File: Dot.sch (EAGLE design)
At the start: 37 parts, among them IC1 CAT24M010TS, IC2 SI1145, U1 ATMEGA328P-MU-QFN32, U2 TMP102, U3 ISL29125, U4 9DoF IMU, U5 BMP18

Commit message: Added voltage divider for input voltage measuring.
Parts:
- added R1, R9: (no value), resistor:R-EU_R0603
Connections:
- new net VIN_PIN: JP1.6, R9.2
- net GND: now also R1.1
- net VIN: now also R1.2, R9.1; no longer JP1.6
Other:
- note added: "Added 100uF Cap."
- note added: "Voltage Divider Lower R"
- note removed: "Added 100uF Cap. Should soften discharge of batetry to peaks up to 30mA for 1ms. Reacharges in 175ms."
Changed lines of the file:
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@@
 <setting verticaltext="up"/>
 </settings>
-<grid distance="0.05" unitdist="inch" unit="inch" style="lines" multiple="1" display="no" altdistance="0.01" altunitdist="inch" altunit="inch"/>
+<grid distance="0.1" unitdist="inch" unit="inch" style="lines" multiple="1" display="no" altdistance="0.01" altunitdist="inch" altunit="inch"/>
 <layers>
 <layer number="1" name="Top" color="4" fill="1" visible="no" active="no"/>
@@
 <part name="SJ2" library="SparkFun" deviceset="SOLDERJUMPER" device="TRACE"/>
 <part name="C5" library="Seeed-OPL-Capacitor" deviceset="TANTALUM-SMD-100UF-6.3V(AVX-A)" device="" value="100uf"/>
+<part name="R1" library="resistor" deviceset="R-EU_" device="R0603"/>
+<part name="SUPPLY16" library="supply2" deviceset="GND" device=""/>
+<part name="R9" library="resistor" deviceset="R-EU_" device="R0603"/>
 </parts>
 <sheets>
@@
 <text x="-7.62" y="50.8" size="1.27" layer="91" rot="R90">Green</text>
 <text x="1.778" y="50.8" size="1.27" layer="91">Red</text>
+<text x="-60.96" y="134.62" size="1.778" layer="91">Voltage Divider Lower R</text>
 </plain>
 <instances>
@@
 <instance part="SJ2" gate="1" x="284.48" y="68.58"/>
 <instance part="C5" gate="G$1" x="2.54" y="162.56" rot="R270"/>
+<instance part="R1" gate="G$1" x="-33.02" y="134.62" rot="R90"/>
+<instance part="SUPPLY16" gate="GND" x="-33.02" y="127"/>
+<instance part="R9" gate="G$1" x="-33.02" y="147.32" rot="R90"/>
 </instances>
 <busses>
@@
 <wire x1="2.54" y1="158.75" x2="10.16" y2="158.75" width="0.1524" layer="91"/>
 <junction x="10.16" y="158.75"/>
+</segment>
+<segment>
+<pinref part="R1" gate="G$1" pin="1"/>
+<pinref part="SUPPLY16" gate="GND" pin="GND"/>
 </segment>
 </net>
@@
 </segment>
 <segment>
-<pinref part="JP1" gate="A" pin="6"/>
-<wire x1="73.66" y1="132.08" x2="86.36" y2="132.08" width="0.1524" layer="91"/>
-<label x="86.36" y="132.08" size="1.27" layer="95" xref="yes"/>
+<pinref part="R9" gate="G$1" pin="1"/>
+<pinref part="R1" gate="G$1" pin="2"/>
+<wire x1="-33.02" y1="142.24" x2="-33.02" y2="139.7" width="0.1524" layer="91"/>
+<wire x1="-33.02" y1="142.24" x2="-27.94" y2="142.24" width="0.1524" layer="91"/>
+<junction x="-33.02" y="142.24"/>
+<label x="-27.94" y="142.24" size="1.27" layer="95" xref="yes"/>
 </segment>
 </net>
@@
 <pinref part="X1" gate="G$1" pin="SIGNAL"/>
 <wire x1="289.56" y1="68.58" x2="292.1" y2="68.58" width="0.1524" layer="91"/>
+</segment>
+</net>
+<net name="VIN_PIN" class="0">
+<segment>
+<pinref part="R9" gate="G$1" pin="2"/>
+<wire x1="-33.02" y1="152.4" x2="-33.02" y2="154.94" width="0.1524" layer="91"/>
+<label x="-33.02" y="154.94" size="1.27" layer="95" xref="yes"/>
+</segment>
+<segment>
+<pinref part="JP1" gate="A" pin="6"/>
+<wire x1="73.66" y1="132.08" x2="86.36" y2="132.08" width="0.1524" layer="91"/>
 </segment>
 </net>
@@
 <text x="-13.97" y="88.9" size="2.54" layer="91">Diff to v1.3</text>
 <text x="-13.462" y="80.01" size="2.1844" layer="91">Corrected RGB Led layout.</text>
-<text x="-12.7" y="73.66" size="2.1844" layer="91">Added 100uF Cap. Should soften discharge of batetry to peaks up to 30mA for 1ms. Reacharges in 175ms.</text>
+<text x="-12.7" y="73.66" size="2.1844" layer="91">Added 100uF Cap.</text>
 </plain>
 <instances>

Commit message: Adding solderjumper for bypassing Voltage Regulator
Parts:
- added SJ3: SOLDERJUMPERNC2, SparkFun:SOLDERJUMPERNC2
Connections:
- net +3V3: now also SJ3.2
- net VIN: now also SJ3.1
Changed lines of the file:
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@@
 <part name="SUPPLY16" library="supply2" deviceset="GND" device=""/>
 <part name="R9" library="resistor" deviceset="R-EU_" device="R0603"/>
+<part name="SJ3" library="SparkFun" deviceset="SOLDERJUMPER" device="NC2"/>
 </parts>
 <sheets>
@@
 RGB Led, Buzzer</text>
 <text x="340.36" y="10.16" size="3.81" layer="95">Antenna Tuning</text>
-<text x="33.02" y="106.68" size="3.81" layer="95">Power and Headers</text>
+<text x="43.18" y="106.68" size="3.81" layer="95">Power and Headers</text>
 <text x="238.76" y="106.68" size="3.81" layer="95">I2C, Reset and Pullups &amp; Push Button(s)</text>
 <text x="-17.78" y="35.56" size="1.778" layer="91">Values @ 20mA.</text>
@@
 <instance part="SUPPLY16" gate="GND" x="-33.02" y="127"/>
 <instance part="R9" gate="G$1" x="-33.02" y="147.32" rot="R90"/>
+<instance part="SJ3" gate="1" x="17.78" y="114.3"/>
 </instances>
 <busses>
@@
 <pinref part="+3V19" gate="G$1" pin="+3V3"/>
 <wire x1="30.48" y1="142.24" x2="30.48" y2="134.62" width="0.1524" layer="91"/>
+<pinref part="SJ3" gate="1" pin="2"/>
+<wire x1="22.86" y1="114.3" x2="30.48" y2="114.3" width="0.1524" layer="91"/>
+<wire x1="30.48" y1="114.3" x2="30.48" y2="134.62" width="0.1524" layer="91"/>
+<junction x="30.48" y="134.62"/>
 </segment>
 <segment>
@@
 <junction x="7.62" y="134.62"/>
 <label x="5.08" y="134.62" size="1.27" layer="95" rot="R180" xref="yes"/>
-</segment>
-<segment>
+<pinref part="SJ3" gate="1" pin="1"/>
+<wire x1="7.62" y1="132.08" x2="7.62" y2="114.3" width="0.1524" layer="91"/>
+<wire x1="7.62" y1="114.3" x2="12.7" y2="114.3" width="0.1524" layer="91"/>
+<junction x="7.62" y="132.08"/>
+</segment>
+<segment>

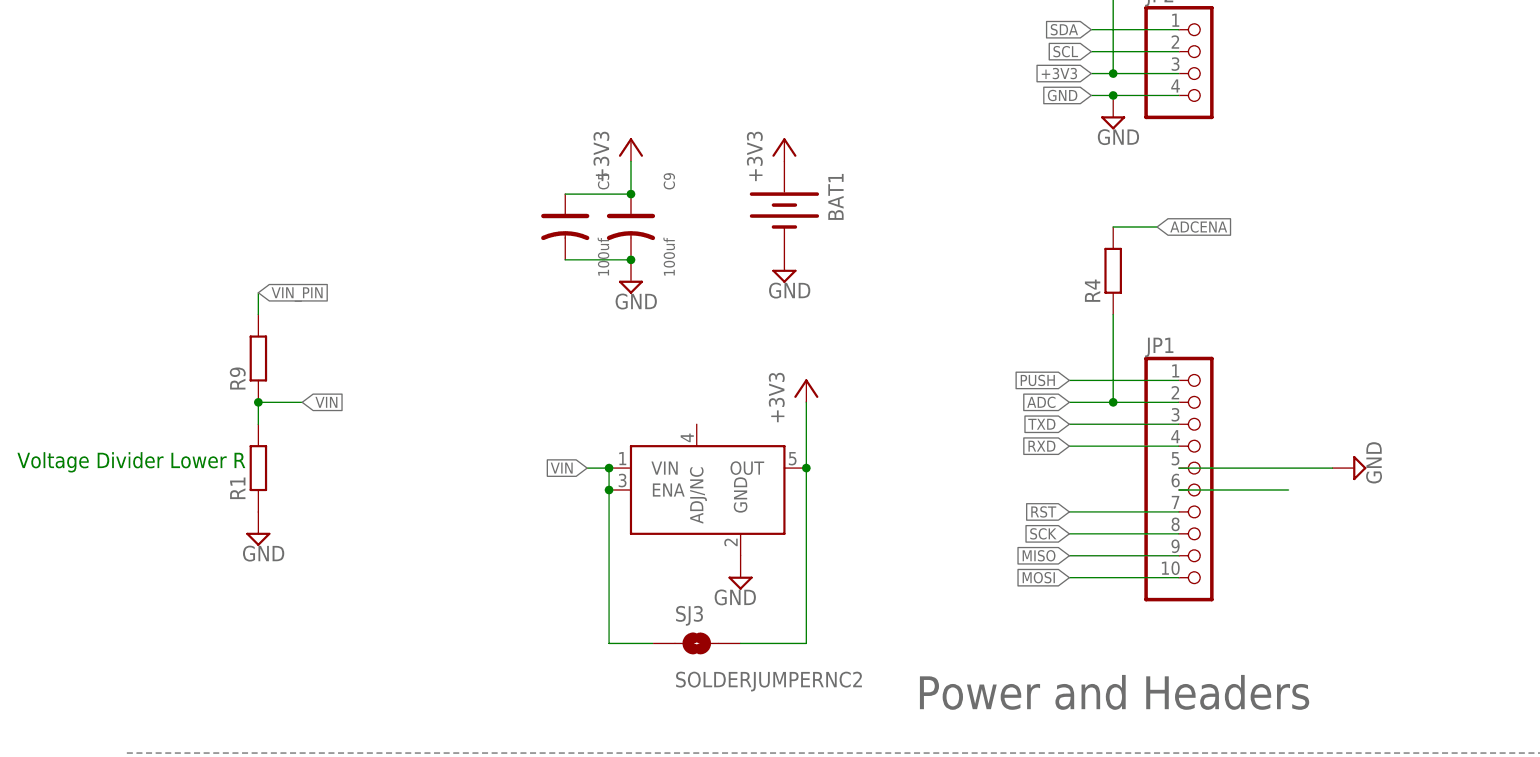
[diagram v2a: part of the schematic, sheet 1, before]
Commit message: Added cap for Reset via DTR pin / Easy Arduino upload
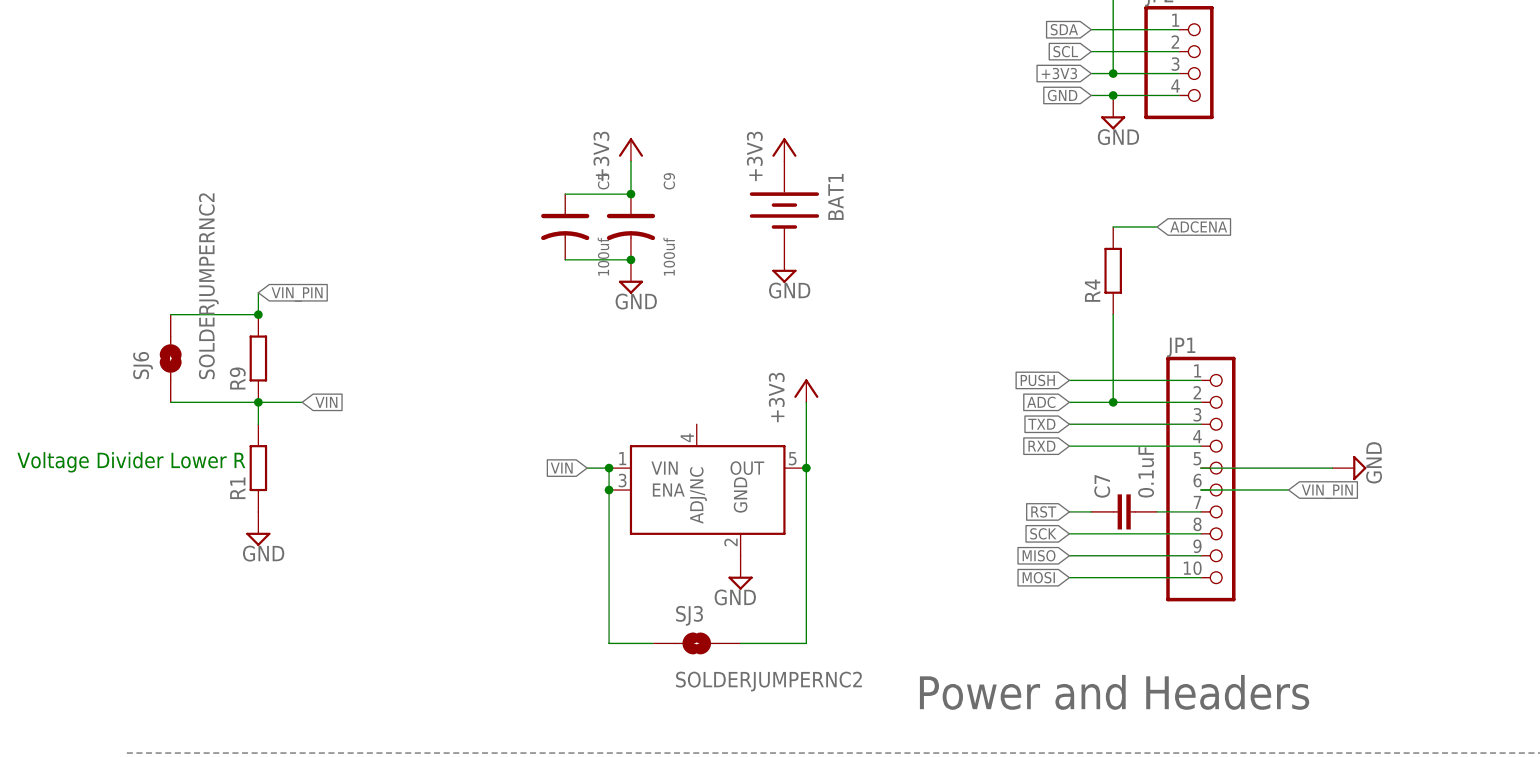
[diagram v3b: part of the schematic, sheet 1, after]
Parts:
- added C7: 0.1uF, resistor:C-EUC0603
- added SJ6: SOLDERJUMPERNC2, SparkFun:SOLDERJUMPERNC2
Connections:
- new net N$5: C7.2, JP1.7
- net RST: now also C7.1; no longer JP1.7
- net VIN: now also SJ6.1
- net VIN_PIN: now also SJ6.2
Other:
- moved on the sheet: JP1
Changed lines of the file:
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@@
 <part name="R9" library="resistor" deviceset="R-EU_" device="R0603"/>
 <part name="SJ3" library="SparkFun" deviceset="SOLDERJUMPER" device="NC2"/>
+<part name="C7" library="resistor" deviceset="C-EU" device="C0603" value="0.1uF"/>
+<part name="SJ6" library="SparkFun" deviceset="SOLDERJUMPER" device="NC2"/>
 </parts>
 <sheets>
@@
 <instance part="SUPPLY13" gate="GND" x="33.02" y="-30.48"/>
 <instance part="SUPPLY19" gate="GND" x="297.18" y="124.46"/>
-<instance part="JP1" gate="A" x="76.2" y="134.62"/>
+<instance part="JP1" gate="A" x="78.74" y="134.62"/>
 <instance part="R5" gate="G$1" x="0" y="60.96" rot="R270"/>
 <instance part="R6" gate="G$1" x="-20.32" y="60.96" rot="R270"/>
@@
 <instance part="R9" gate="G$1" x="-33.02" y="147.32" rot="R90"/>
 <instance part="SJ3" gate="1" x="17.78" y="114.3"/>
+<instance part="C7" gate="G$1" x="66.04" y="129.54" rot="R90"/>
+<instance part="SJ6" gate="1" x="-43.18" y="147.32" rot="R90"/>
 </instances>
 <busses>
@@
 <segment>
 <pinref part="SUPPLY1" gate="GND" pin="GND"/>
-<wire x1="73.66" y1="134.62" x2="91.44" y2="134.62" width="0.1524" layer="91"/>
+<wire x1="76.2" y1="134.62" x2="91.44" y2="134.62" width="0.1524" layer="91"/>
 <pinref part="JP1" gate="A" pin="5"/>
 </segment>
@@
 <net name="RST" class="0">
 <segment>
-<label x="60.96" y="129.54" size="1.27" layer="95" rot="R180" xref="yes"/>
-<wire x1="60.96" y1="129.54" x2="73.66" y2="129.54" width="0.1524" layer="91"/>
-<pinref part="JP1" gate="A" pin="7"/>
-</segment>
-<segment>
 <pinref part="U1" gate="G$1" pin="PC6(PCINT14/!RESET)"/>
 <wire x1="195.58" y1="43.18" x2="198.12" y2="43.18" width="0.1524" layer="91"/>
@@
 <wire x1="269.24" y1="154.94" x2="251.46" y2="154.94" width="0.1524" layer="91"/>
 <label x="251.46" y="154.94" size="1.27" layer="95" rot="R180" xref="yes"/>
+</segment>
+<segment>
+<pinref part="C7" gate="G$1" pin="1"/>
+<wire x1="63.5" y1="129.54" x2="60.96" y2="129.54" width="0.1524" layer="91"/>
+<label x="60.96" y="129.54" size="1.27" layer="95" rot="R180" xref="yes"/>
 </segment>
 </net>
@@
 <segment>
 <label x="60.96" y="121.92" size="1.27" layer="95" rot="R180" xref="yes"/>
-<wire x1="60.96" y1="121.92" x2="73.66" y2="121.92" width="0.1524" layer="91"/>
+<wire x1="60.96" y1="121.92" x2="76.2" y2="121.92" width="0.1524" layer="91"/>
 <pinref part="JP1" gate="A" pin="10"/>
 </segment>
@@
 <segment>
 <label x="60.96" y="124.46" size="1.27" layer="95" rot="R180" xref="yes"/>
-<wire x1="60.96" y1="124.46" x2="73.66" y2="124.46" width="0.1524" layer="91"/>
+<wire x1="60.96" y1="124.46" x2="76.2" y2="124.46" width="0.1524" layer="91"/>
 <pinref part="JP1" gate="A" pin="9"/>
 </segment>
@@
 <segment>
 <pinref part="JP1" gate="A" pin="3"/>
-<wire x1="73.66" y1="139.7" x2="60.96" y2="139.7" width="0.1524" layer="91"/>
+<wire x1="76.2" y1="139.7" x2="60.96" y2="139.7" width="0.1524" layer="91"/>
 <label x="60.96" y="139.7" size="1.27" layer="95" rot="R180" xref="yes"/>
 </segment>
@@
 </segment>
 <segment>
-<wire x1="73.66" y1="127" x2="60.96" y2="127" width="0.1524" layer="91"/>
+<wire x1="76.2" y1="127" x2="60.96" y2="127" width="0.1524" layer="91"/>
 <label x="60.96" y="127" size="1.27" layer="95" rot="R180" xref="yes"/>
 <pinref part="JP1" gate="A" pin="8"/>
@@
 <segment>
 <pinref part="JP1" gate="A" pin="1"/>
-<wire x1="73.66" y1="144.78" x2="60.96" y2="144.78" width="0.1524" layer="91"/>
+<wire x1="76.2" y1="144.78" x2="60.96" y2="144.78" width="0.1524" layer="91"/>
 <label x="60.96" y="144.78" size="1.27" layer="95" rot="R180" xref="yes"/>
 </segment>
@@
 <segment>
 <pinref part="JP1" gate="A" pin="4"/>
-<wire x1="73.66" y1="137.16" x2="60.96" y2="137.16" width="0.1524" layer="91"/>
+<wire x1="76.2" y1="137.16" x2="60.96" y2="137.16" width="0.1524" layer="91"/>
 <label x="60.96" y="137.16" size="1.27" layer="95" rot="R180" xref="yes"/>
 </segment>
@@
 <segment>
 <pinref part="JP1" gate="A" pin="2"/>
-<wire x1="73.66" y1="142.24" x2="66.04" y2="142.24" width="0.1524" layer="91"/>
+<wire x1="76.2" y1="142.24" x2="66.04" y2="142.24" width="0.1524" layer="91"/>
 <label x="60.96" y="142.24" size="1.27" layer="95" rot="R180" xref="yes"/>
 <pinref part="R4" gate="G$1" pin="1"/>
@@
 <junction x="-33.02" y="142.24"/>
 <label x="-27.94" y="142.24" size="1.27" layer="95" xref="yes"/>
+<pinref part="SJ6" gate="1" pin="1"/>
+<wire x1="-43.18" y1="142.24" x2="-33.02" y2="142.24" width="0.1524" layer="91"/>
 </segment>
 </net>
@@
 <wire x1="-33.02" y1="152.4" x2="-33.02" y2="154.94" width="0.1524" layer="91"/>
 <label x="-33.02" y="154.94" size="1.27" layer="95" xref="yes"/>
+<pinref part="SJ6" gate="1" pin="2"/>
+<wire x1="-43.18" y1="152.4" x2="-33.02" y2="152.4" width="0.1524" layer="91"/>
+<junction x="-33.02" y="152.4"/>
 </segment>
 <segment>
 <pinref part="JP1" gate="A" pin="6"/>
-<wire x1="73.66" y1="132.08" x2="86.36" y2="132.08" width="0.1524" layer="91"/>
-</segment>
-</net>
+<wire x1="76.2" y1="132.08" x2="86.36" y2="132.08" width="0.1524" layer="91"/>
+<label x="86.36" y="132.08" size="1.27" layer="95" xref="yes"/>
+</segment>
+</net>
+<net name="N$5" class="0">
+<segment>
+<pinref part="JP1" gate="A" pin="7"/>
+<pinref part="C7" gate="G$1" pin="2"/>
+<wire x1="76.2" y1="129.54" x2="71.12" y2="129.54" width="0.1524" layer="91"/>
+</segment>
+</net>

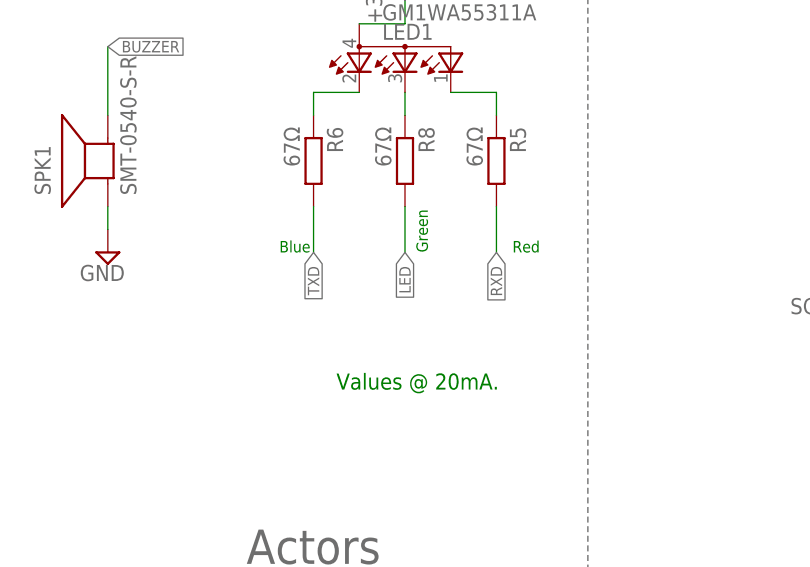
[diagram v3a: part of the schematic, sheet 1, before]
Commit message: Update led : G(TxD) B(RxD) R(LED)
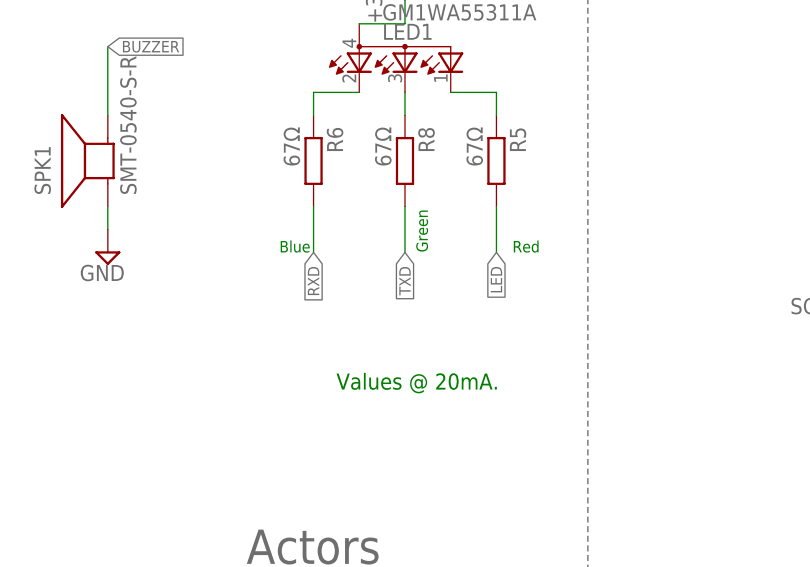
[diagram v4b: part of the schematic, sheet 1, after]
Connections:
- net LED: now also R5.2; no longer R8.2
- net RXD: now also R6.2; no longer R5.2
- net TXD: now also R8.2; no longer R6.2

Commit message: Add pullup to UV, RGB and Temp. Their IRQ share same line
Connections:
- removed net INT_RGB: U1.PB6(XTAL1/TOSC1/PCINT6), U3.!INT
- removed net INT_UV: IC2.INT, U1.PB7(XTAL2/TOSC2/PCINT7)
- removed net TEMP_ALERT: U1.PB2(SS/OC1B/PCINT2), U2.ALERT
- new net INT_MULTIPLE: IC2.INT, R7A.1, U1.PB7(XTAL2/TOSC2/PCINT7), U2.ALERT, U3.!INT
- net +3V3: now also R7A.2
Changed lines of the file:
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@@
 <pinref part="R7" gate="C" pin="2"/>
 <wire x1="297.18" y1="149.86" x2="297.18" y2="154.94" width="0.1524" layer="91"/>
-<wire x1="297.18" y1="154.94" x2="297.18" y2="165.1" width="0.1524" layer="91"/>
+<wire x1="297.18" y1="154.94" x2="297.18" y2="160.02" width="0.1524" layer="91"/>
+<wire x1="297.18" y1="160.02" x2="297.18" y2="165.1" width="0.1524" layer="91"/>
 <wire x1="279.4" y1="149.86" x2="297.18" y2="149.86" width="0.1524" layer="91"/>
 <junction x="297.18" y="149.86"/>
@@
 <wire x1="279.4" y1="154.94" x2="297.18" y2="154.94" width="0.1524" layer="91"/>
 <junction x="297.18" y="154.94"/>
+<pinref part="R7" gate="A" pin="2"/>
+<wire x1="279.4" y1="160.02" x2="297.18" y2="160.02" width="0.1524" layer="91"/>
+<junction x="297.18" y="160.02"/>
 </segment>
 <segment>
@@
 </segment>
 </net>
-<net name="TEMP_ALERT" class="0">
-<segment>
-<pinref part="U2" gate="G$1" pin="ALERT"/>
-<wire x1="185.42" y1="-15.24" x2="187.96" y2="-15.24" width="0.1524" layer="91"/>
-<label x="187.96" y="-15.24" size="1.27" layer="95" xref="yes"/>
-</segment>
-<segment>
-<pinref part="U1" gate="G$1" pin="PB2(SS/OC1B/PCINT2)"/>
-<wire x1="195.58" y1="81.28" x2="198.12" y2="81.28" width="0.1524" layer="91"/>
-<label x="198.12" y="81.28" size="1.27" layer="95" xref="yes"/>
-</segment>
-</net>
 <net name="MOVE_INT" class="0">
 <segment>
@@
 <wire x1="195.58" y1="53.34" x2="198.12" y2="53.34" width="0.1524" layer="91"/>
 <label x="198.12" y="53.34" size="1.27" layer="95" xref="yes"/>
-</segment>
-</net>
-<net name="INT_RGB" class="0">
-<segment>
-<pinref part="U3" gate="G$1" pin="!INT"/>
-<wire x1="368.3" y1="-30.48" x2="370.84" y2="-30.48" width="0.1524" layer="91"/>
-<label x="370.84" y="-30.48" size="1.27" layer="95" xref="yes"/>
-</segment>
-<segment>
-<pinref part="U1" gate="G$1" pin="PB6(XTAL1/TOSC1/PCINT6)"/>
-<wire x1="195.58" y1="68.58" x2="198.12" y2="68.58" width="0.1524" layer="91"/>
-<label x="198.12" y="68.58" size="1.27" layer="95" xref="yes"/>
-</segment>
-</net>
-<net name="INT_UV" class="0">
-<segment>
-<pinref part="IC2" gate="G$1" pin="INT"/>
-<wire x1="264.16" y1="-30.48" x2="261.62" y2="-30.48" width="0.1524" layer="91"/>
-<label x="261.62" y="-30.48" size="1.27" layer="95" rot="R180" xref="yes"/>
-</segment>
-<segment>
-<pinref part="U1" gate="G$1" pin="PB7(XTAL2/TOSC2/PCINT7)"/>
-<wire x1="195.58" y1="63.5" x2="198.12" y2="63.5" width="0.1524" layer="91"/>
-<label x="198.12" y="63.5" size="1.27" layer="95" xref="yes"/>
 </segment>
 </net>
@@
 </segment>
 </net>
+<net name="INT_MULTIPLE" class="0">
+<segment>
+<pinref part="R7" gate="A" pin="1"/>
+<wire x1="269.24" y1="160.02" x2="251.46" y2="160.02" width="0.1524" layer="91"/>
+<label x="251.46" y="160.02" size="1.27" layer="95" rot="R180" xref="yes"/>
+</segment>
+<segment>
+<pinref part="U1" gate="G$1" pin="PB7(XTAL2/TOSC2/PCINT7)"/>
+<wire x1="195.58" y1="63.5" x2="198.12" y2="63.5" width="0.1524" layer="91"/>
+<label x="198.12" y="63.5" size="1.27" layer="95" xref="yes"/>
+</segment>
+<segment>
+<pinref part="U2" gate="G$1" pin="ALERT"/>
+<wire x1="185.42" y1="-15.24" x2="187.96" y2="-15.24" width="0.1524" layer="91"/>
+<label x="187.96" y="-15.24" size="1.27" layer="95" xref="yes"/>
+</segment>
+<segment>
+<pinref part="IC2" gate="G$1" pin="INT"/>
+<wire x1="264.16" y1="-30.48" x2="261.62" y2="-30.48" width="0.1524" layer="91"/>
+<label x="261.62" y="-30.48" size="1.27" layer="95" rot="R180" xref="yes"/>
+</segment>
+<segment>
+<pinref part="U3" gate="G$1" pin="!INT"/>
+<wire x1="368.3" y1="-30.48" x2="370.84" y2="-30.48" width="0.1524" layer="91"/>
+<label x="370.84" y="-30.48" size="1.27" layer="95" xref="yes"/>
+</segment>
+</net>
